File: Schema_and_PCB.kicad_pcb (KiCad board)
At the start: 4 copper layers, 293.6 x 143.3 mm, 216 parts, among them J1 USB4085-GF-A_REVA, J11 Pulse_JXD6-0001NL, J12 OSTTC020162, J13 640456-2, J14 640456-3, J15 640456-3, J16 0022232041, J17 0022232041, J2 OSTTC020162, J3 302-S101, J4 DM3AT-SF-PEJM5, J5 OSTTC020162, J7 OSTTC030162, J9 0022232031, Q1 BC817-25LT1G, Q2 BC817-25LT1G, Q3 BC817-25LT1G, Q4 BC817-25LT1G, SW1 SW_PUSHBUTTON, SW2 SW_PUSHBUTTON, SW3 SW_PUSHBUTTON, SW4 SW_PUSHBUTTON, SW5 SW_PUSHBUTTON, SW6 SW_PUSHBUTTON, U1 CC56-12SURKWA, U10 TLV75529PDBV, U11 STM32H743ZIT6, U12 LD1117S33CTR, U13 LD1117S33CTR, U14 SN74AVCA406DGGR, U15 W25Q256JVFIQ, U17 ISO1211DR, U2 CC56-12SURKWA, U24 ISO1211DR, U26 ISO1211DR, U3 MAX7219EWG+T, U30 LAN8742A-CZ-TR, U4 BC56-12SURKWA, U5 SC56-11SRWA, U6 MAX7219EWG+T, U7 CC56-12SURKWA, U8 ADUM4160, U9 ST1L05APU33R, Y1 NX5032GA-8MHz, Y2 NX3215SA-32.768K-STD-MUA-14, Y3 NX2016SA-25MHz

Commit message: main PCB changes
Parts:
- C21, C48, C49, C50: moved to B.Cu
- moved C35 240.0 mm to (50.9, 134.1)
- moved J17 113.3 mm to (160.9, 73.4)
- moved C39 102.0 mm to (50.1, 141.1)
- moved C44 93.6 mm to (52.9, 129.3)
- moved C40 83.5 mm to (53.1, 126.3), turned to 180 degrees
- moved C37 66.3 mm to (49.8, 137.4), turned to 180 degrees
- moved C42 60.3 mm to (58.0, 126.2)
- moved C41 59.2 mm to (58.0, 129.4)
- moved C43 55.0 mm to (58.0, 132.6)
- moved C28 34.3 mm to (157.3, 92.2)
- moved C23 32.6 mm to (128.3, 154.7), turned to 270 degrees
- moved C50 31.4 mm to (133.3, 132.9), turned to 270 degrees
- moved C22 30.3 mm to (116.6, 143.5), turned to 180 degrees
- moved C19 30.2 mm to (116.7, 132.0), turned to 180 degrees
- moved C18 30.1 mm to (116.6, 138.5), turned to 180 degrees
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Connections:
- J3 pad 8: /Digital_IO_analog_Inputs/ADC3_P -> /Digital_IO_analog_Inputs/A_CH1_FAULT
- U11 pad 49: /Digital_IO_analog_Inputs/ADC3_P -> /Digital_IO_analog_Inputs/A_CH1_FAULT
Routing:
- net Net-(C6-Pad2): track 0.00 -> 9.21 mm
- net Net-(C5-Pad2): track 0.00 -> 8.91 mm
- net Net-(C7-Pad2): track 0.00 -> 6.35 mm
- net Net-(C10-Pad2): track 0.00 -> 5.51 mm
- net GNDREF: track 0.00 -> 3.36 mm, vias 8 -> 11
- net (no net): vias 1 -> 0

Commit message: Footprints for pinheaders changed
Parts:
- J12: value OSTTC020162 -> Ground; footprint digikey-footprints:Term_Block_1x2_P5mm -> Connector_PinHeader_2.54mm:PinHeader_1x01_P2.54mm_Vertical
- moved C37 93.3 mm to (130.3, 90.3), turned to 0 degrees
- moved C35 79.8 mm to (126.1, 107.5), turned to 270 degrees
- moved BT1 72.3 mm to (253.4, 86.2)
- moved JP1 64.2 mm to (137.8, 134.9), turned to 180 degrees
- moved JP5 28.1 mm to (116.7, 125.5)
- moved C34 27.6 mm to (116.0, 128.7), turned to 180 degrees
- moved R18 25.5 mm to (114.7, 121.2), turned to 90 degrees
- moved R22 23.3 mm to (132.3, 107.5), turned to 90 degrees
- moved R19 21.4 mm to (135.7, 107.5), turned to 90 degrees
- moved J12 17.3 mm to (67.8, 166.9)
- moved R20 10.2 mm to (123.5, 107.5), turned to 90 degrees
- moved R21 10.1 mm to (120.4, 107.6), turned to 90 degrees
- moved U9 3.90 mm to (77.8, 129.5)
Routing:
- added copper zone on F.Cu, net Net-(U24-Pad5)
- added copper zone on F.Cu, net Net-(U26-Pad5)

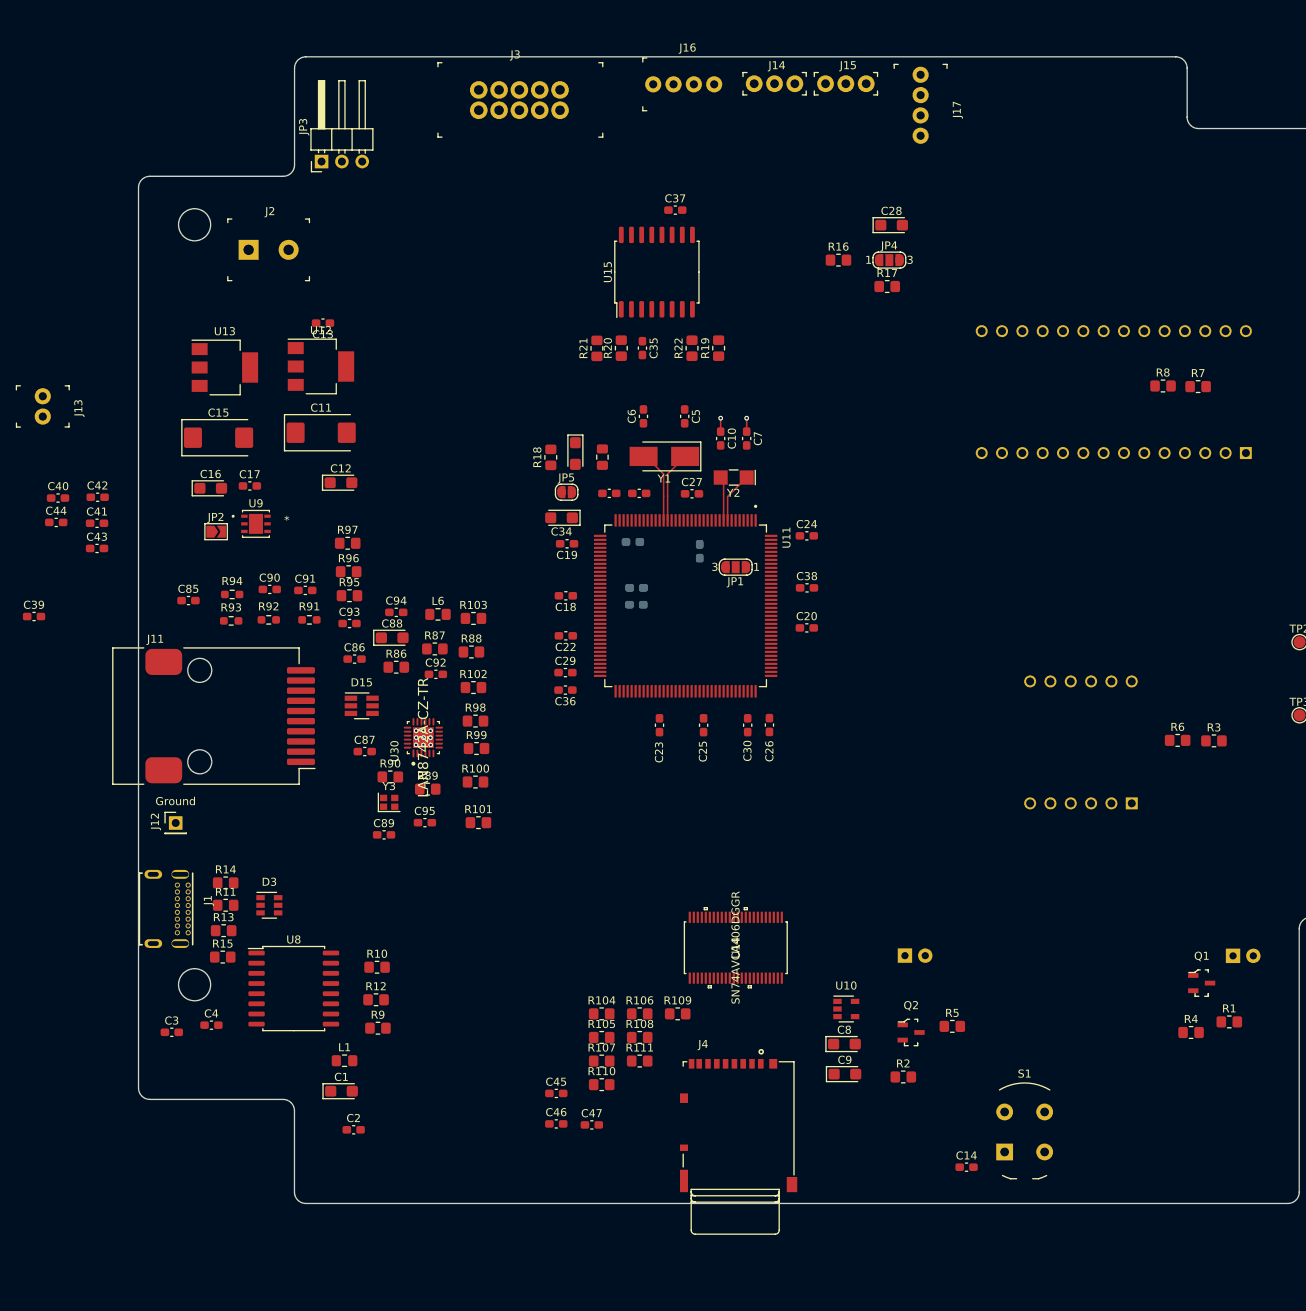
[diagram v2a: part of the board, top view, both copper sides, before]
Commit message: LAN elements placed
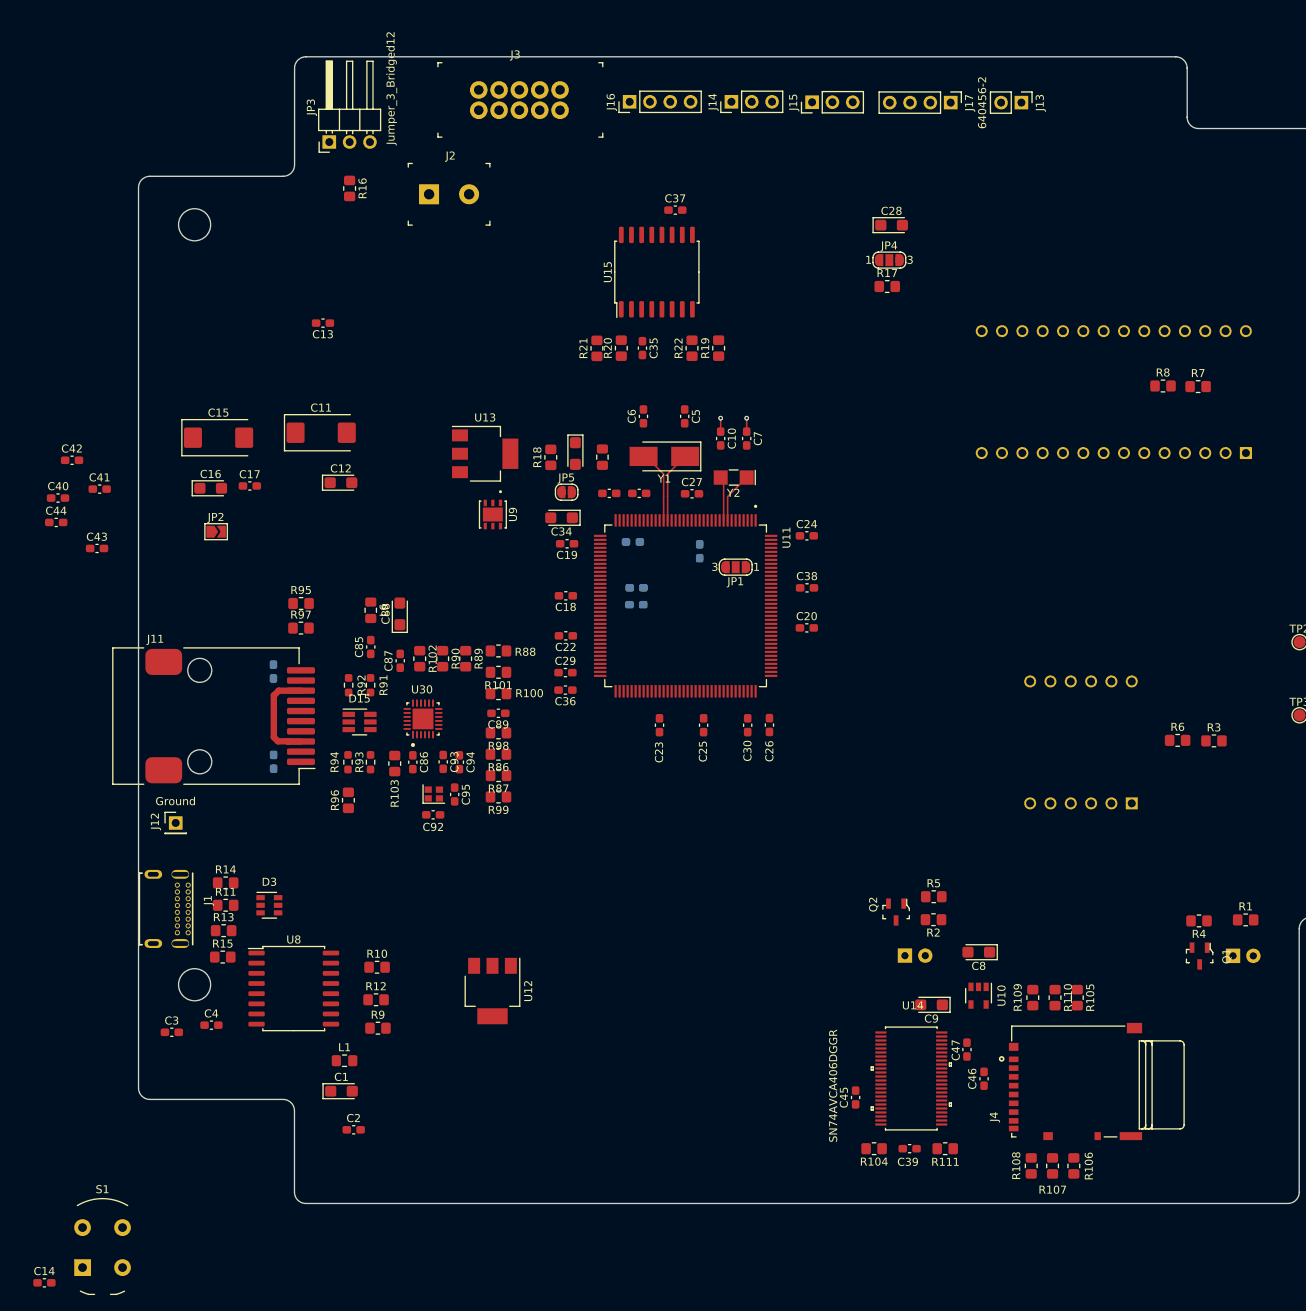
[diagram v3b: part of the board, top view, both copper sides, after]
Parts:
- C90, C91: moved to B.Cu
- J13: footprint digikey-footprints:PinHeader_1x2_P2.54mm_Drill1.02mm -> Connector_PinHeader_2.54mm:PinHeader_1x02_P2.54mm_Vertical
- J14, J15: footprint digikey-footprints:PinHeader_1x3_P2.54_Drill1.1mm -> Connector_PinHeader_2.54mm:PinHeader_1x03_P2.54mm_Vertical
- J16, J17: footprint digikey-footprints:PinHeader_1x4_P2.54mm_Drill1.02mm -> Connector_PinHeader_2.54mm:PinHeader_1x04_P2.54mm_Vertical
- moved C39 128.1 mm to (159.5, 207.6)
- moved J13 127.7 mm to (173.5, 76.8)
- moved C14 116.2 mm to (51.4, 224.4)
- moved S1 116.2 mm to (56.1, 222.5)
- moved U12 81.0 mm to (107.4, 187.9), turned to 270 degrees
- moved R16 61.8 mm to (89.5, 87.6), turned to 270 degrees
- moved R105 59.7 mm to (180.5, 188.7), turned to 270 degrees
- moved R107 57.9 mm to (177.4, 209.7), turned to 90 degrees
- moved R110 57.7 mm to (177.7, 188.7), turned to 270 degrees
- moved R106 57.5 mm to (180.1, 209.7), turned to 90 degrees
- moved C46 53.8 mm to (168.8, 198.9), turned to 90 degrees
- moved R108 51.5 mm to (174.7, 209.7), turned to 90 degrees
- moved C47 47.8 mm to (166.7, 195.2), turned to 90 degrees
- moved R109 44.4 mm to (174.9, 188.7), turned to 270 degrees
- moved R111 39.7 mm to (164.0, 207.6)
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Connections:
- C47 pad 1: GNDREF -> +2,9V
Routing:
- net Net-(C85-Pad2): track 0.00 -> 12.5 mm
- net GNDREF: vias 11 -> 2

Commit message: ISO1211 power supply apdated. Label USB_GND added
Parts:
- added C51: 10µFx16, Capacitor_Tantalum_SMD:CP_EIA-3216-10_Kemet-I, F.Cu at (316.8, 123.2)
- added C52: 1µF, Capacitor_SMD:C_0603_1608Metric_Pad1.08x0.95mm_HandSolder, F.Cu at (323.6, 151.5)
- added L3: 600R@100MHz, Inductor_SMD:L_0805_2012Metric_Pad1.15x1.40mm_HandSolder, F.Cu at (137.8, 186.4)
- R15: moved to B.Cu
- moved J2 116.7 mm to (125.2, 202.2)
- moved S1 115.1 mm to (73.8, 108.8)
- moved C14 110.3 mm to (75.7, 116.8), turned to 180 degrees
- moved C12 95.8 mm to (119.3, 215.0)
- moved JP2 95.8 mm to (103.7, 221.2)
- moved U9 95.8 mm to (138.3, 219.0)
- moved C11 95.8 mm to (116.8, 208.8)
- moved C15 95.8 mm to (104.0, 209.4)
- moved C16 95.8 mm to (103.0, 215.7)
- moved C17 95.8 mm to (107.9, 215.5)
- moved C13 95.8 mm to (117.1, 195.1)
- moved U13 95.8 mm to (137.3, 211.4)
- moved C3 17.7 mm to (81.9, 182.9), turned to 270 degrees
- moved U12 16.2 mm to (123.5, 189.4)
- moved U8 12.5 mm to (90.4, 177.8)
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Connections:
- C69 pad 1: VDD_PER -> Net-(C51-Pad1)
- C75 pad 1: VDD_PER -> Net-(C51-Pad1)
- U17 pad 1: VDD_PER -> Net-(C51-Pad1)
- U17 pad 2: VDD_PER -> Net-(C51-Pad1)
- U24 pad 1: VDD_PER -> Net-(C51-Pad1)
- U24 pad 2: VDD_PER -> Net-(C51-Pad1)
- U26 pad 1: VDD_PER -> Net-(C51-Pad1)
- U26 pad 2: VDD_PER -> Net-(C51-Pad1)

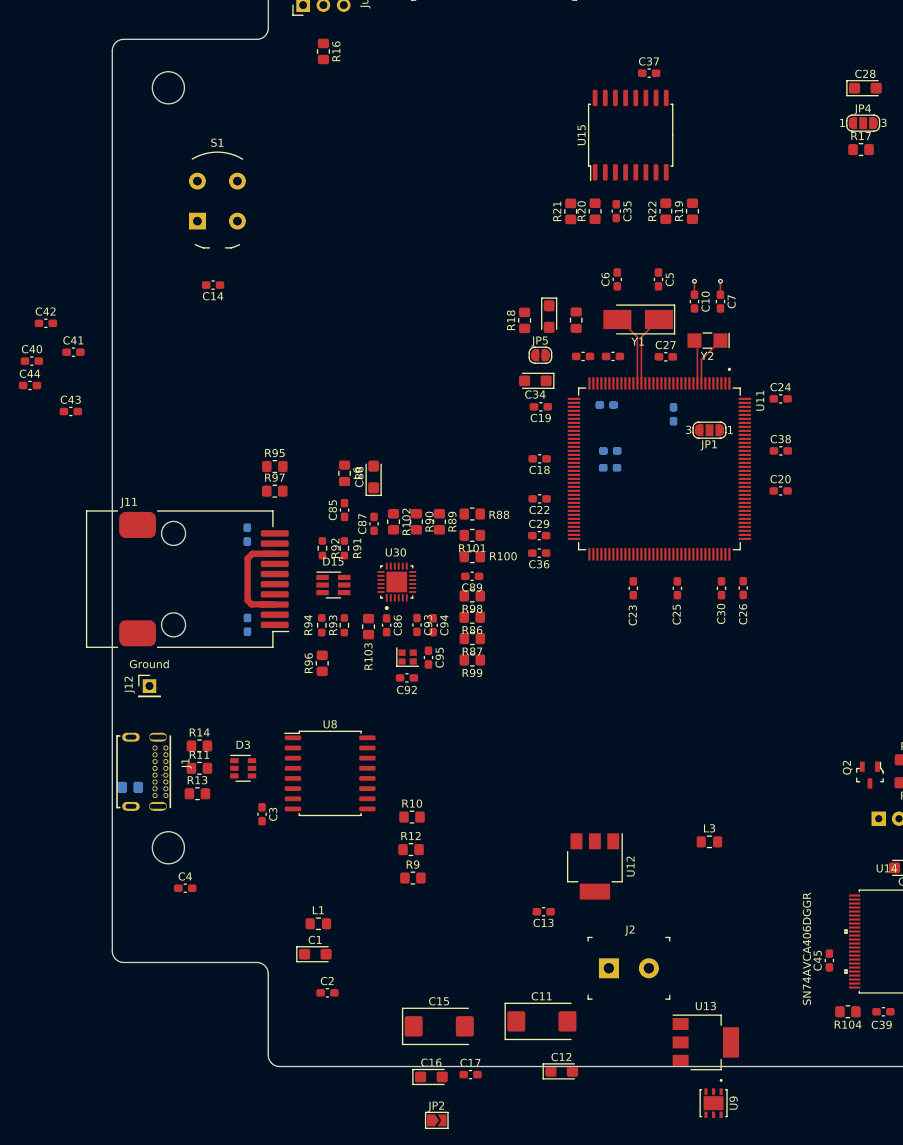
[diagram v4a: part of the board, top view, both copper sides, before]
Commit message: PCB autorouting attempt
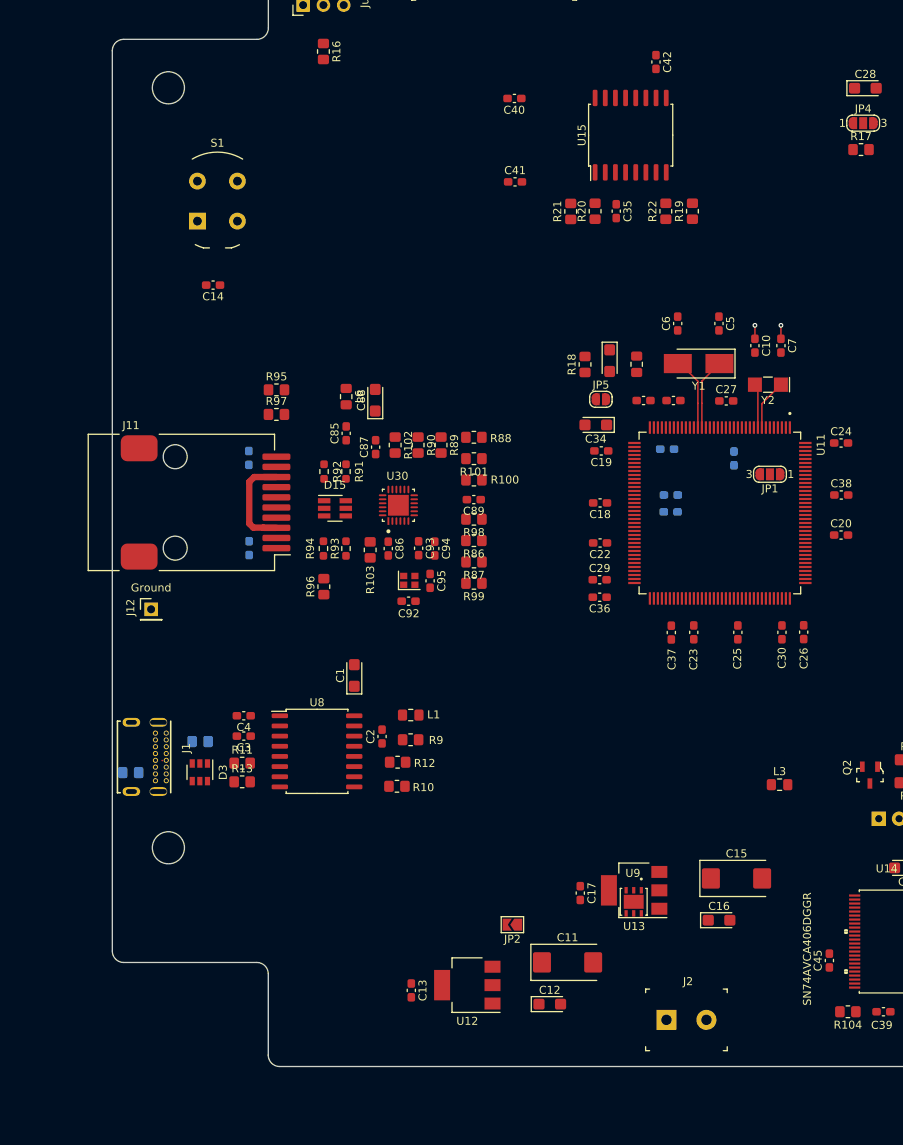
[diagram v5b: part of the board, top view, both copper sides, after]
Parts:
- removed C43, C44: 1µF, Capacitor_SMD:C_0603_1608Metric_Pad1.08x0.95mm_HandSolder
- R14: moved to B.Cu
- moved C42 83.0 mm to (131.1, 88.9), turned to 270 degrees
- moved C37 70.0 mm to (133.0, 160.2), turned to 270 degrees
- moved C40 68.7 mm to (113.4, 93.4), turned to 0 degrees
- moved C41 59.2 mm to (113.5, 103.9)
- moved C15 41.5 mm to (141.2, 190.9)
- moved C16 41.0 mm to (139.0, 196.2)
- moved C1 35.2 mm to (93.4, 165.6), turned to 90 degrees
- moved C2 32.8 mm to (96.9, 173.2), turned to 90 degrees
- moved L1 28.5 mm to (100.4, 170.5), turned to 180 degrees
- moved U9 27.1 mm to (128.3, 193.9)
- moved C17 26.5 mm to (121.6, 192.8), turned to 270 degrees
- moved JP2 26.2 mm to (113.2, 196.7), turned to 180 degrees
- moved C4 22.8 mm to (79.6, 170.6), turned to 180 degrees
- moved U12 21.8 mm to (107.5, 204.3), turned to 180 degrees
- moved U13 21.0 mm to (128.4, 192.4), turned to 180 degrees
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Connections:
- net Net-(C3-Pad2) renamed /USB/USB_GND
- net Net-(C4-Pad1) renamed /USB/USB_VBUS
- net Net-(D3-Pad3) renamed /USB/USB_DP
- net Net-(D3-Pad4) renamed /USB/USB_DN

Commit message: PCB drawing
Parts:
- moved Y3 0.71 mm to (99.6, 153.7)
- moved C95 0.71 mm to (102.2, 153.7)
- moved C92 0.71 mm to (99.5, 156.3)
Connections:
- net Net-(C85-Pad2) renamed /LAN/LAN_PWR
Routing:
- net /LAN/LAN_PWR: track 12.5 -> 54.1 mm, vias 0 -> 2
- net GNDREF: track 3.36 -> 25.7 mm, vias 2 -> 11
- net /LAN/TD_N: track 0.00 -> 19.0 mm, vias 0 -> 3
- net Net-(J11-Pad2): track 0.00 -> 18.7 mm
- net /LAN/RD_N: track 0.04 -> 17.5 mm
- net VDD_MCU: track 0.00 -> 12.5 mm
- net Net-(R87-Pad2): track 0.00 -> 11.6 mm
- net Net-(C92-Pad1): track 0.00 -> 11.2 mm
- net /LAN/TD_P: track 0.00 -> 9.27 mm
- net Net-(C6-Pad2): track 9.21 -> 0.00 mm
- net Net-(C95-Pad1): track 0.00 -> 9.06 mm
- net Net-(C5-Pad2): track 8.91 -> 0.00 mm
- net /LAN/RD_P: track 0.00 -> 8.89 mm
- net Net-(R101-Pad2): track 0.00 -> 8.57 mm
- net Net-(R100-Pad1): track 0.00 -> 7.67 mm
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
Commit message: PCB layout
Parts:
- C21, C48, C49: moved to F.Cu
- JP2: footprint Jumper:SolderJumper-2_P1.3mm_Open_TrianglePad1.0x1.5mm -> Connector_PinHeader_2.54mm:PinHeader_1x02_P2.54mm_Vertical
- R3, R6: moved to B.Cu
- moved R74 206.9 mm to (117.3, 170.3)
- moved R75 177.7 mm to (125.1, 174.5)
- moved R76 155.0 mm to (125.8, 165.7)
- moved R77 132.5 mm to (125.8, 170.3)
- moved R78 104.4 mm to (132.0, 174.0)
- moved R79 75.4 mm to (138.8, 173.8)
- moved R3 26.7 mm to (223.0, 148.5), turned to 180 degrees
- moved R6 25.9 mm to (217.7, 148.5), turned to 180 degrees
- moved R21 20.0 mm to (135.8, 94.8), turned to 270 degrees
- moved JP1 17.3 mm to (157.7, 128.2)
- moved C40 17.2 mm to (129.7, 98.8)
- moved C41 17.2 mm to (129.8, 109.2)
- moved R19 13.0 mm to (146.6, 100.5)
- moved C42 12.6 mm to (142.2, 95.0)
- moved C35 12.6 mm to (137.2, 113.6)
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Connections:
- net /USB/USB_DN renamed /USB/USB_D_N
- net /USB/USB_DP renamed /USB/USB_D_P
- net Net-(C66-Pad1) renamed /Digital_IO_analog_Inputs/ENCODER_IN_A
- net Net-(C66-Pad2) renamed /Digital_IO_analog_Inputs/COM_ENCODER
- R74 pad 1: VDD_PER -> VDD_MCU
- R75 pad 1: VDD_PER -> VDD_MCU
- R76 pad 1: VDD_PER -> VDD_MCU
- R77 pad 1: VDD_PER -> VDD_MCU
- R78 pad 1: VDD_PER -> VDD_MCU
- R79 pad 1: VDD_PER -> VDD_MCU
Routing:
- net GNDREF: track 25.7 -> 241.7 mm, vias 11 -> 75
- net +5V: track 0.00 -> 205.3 mm
- net VDD_MCU: track 12.5 -> 151.0 mm, vias 0 -> 36
- net VDD_PER: track 0.00 -> 85.7 mm, vias 0 -> 13
- net /Microcontroller/USB_FS_DP: track 0.00 -> 63.2 mm
- net +2,9V: track 0.00 -> 62.4 mm
- net /Microcontroller/USB_FS_DN: track 0.00 -> 62.3 mm
- net NRST: track 0.00 -> 60.6 mm
- net Net-(J4-Pad5): track 0.00 -> 31.3 mm, vias 0 -> 2
- net /USB/USB_GND: track 0.00 -> 28.2 mm, vias 0 -> 6
- net /LAN/RMII_RXD1: track 0.00 -> 28.0 mm
- net Net-(J11-Pad10): track 0.00 -> 26.0 mm, vias 0 -> 2
- net /USB/USB_VBUS: track 0.00 -> 25.1 mm
- net Net-(J4-Pad2): track 0.00 -> 24.3 mm, vias 0 -> 2
- net Net-(J4-Pad3): track 0.00 -> 24.1 mm, vias 0 -> 2
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- added copper zone on GND, net /Digital_IO_analog_Inputs/COM_ENCODER
- added copper zone on POWER, net /LAN/LAN_PWR
- added copper zone on GND, net /USB/USB_GND
- added copper zone on GND, net GNDREF
- added copper zone on F.Cu, net Net-(U10-Pad4)
- added copper zone on POWER, net VDD_MCU
- added copper zone on F.Cu, net VDD_PER
- added copper zone on POWER, net VDD_PER
